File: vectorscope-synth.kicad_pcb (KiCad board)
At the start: 2 copper layers, 116 x 73 mm, 25 parts, among them J1 STYLUS, J2 IO CONNECTOR, J2OUT IO CONNECTOR, J3 SCOPE, J3OUT SCOPE, J4 SIGGEN, J4OUT SIGGEN, J5 PATCH SELECT, J6 WRITE PATCH, J7 PARAM SELECT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

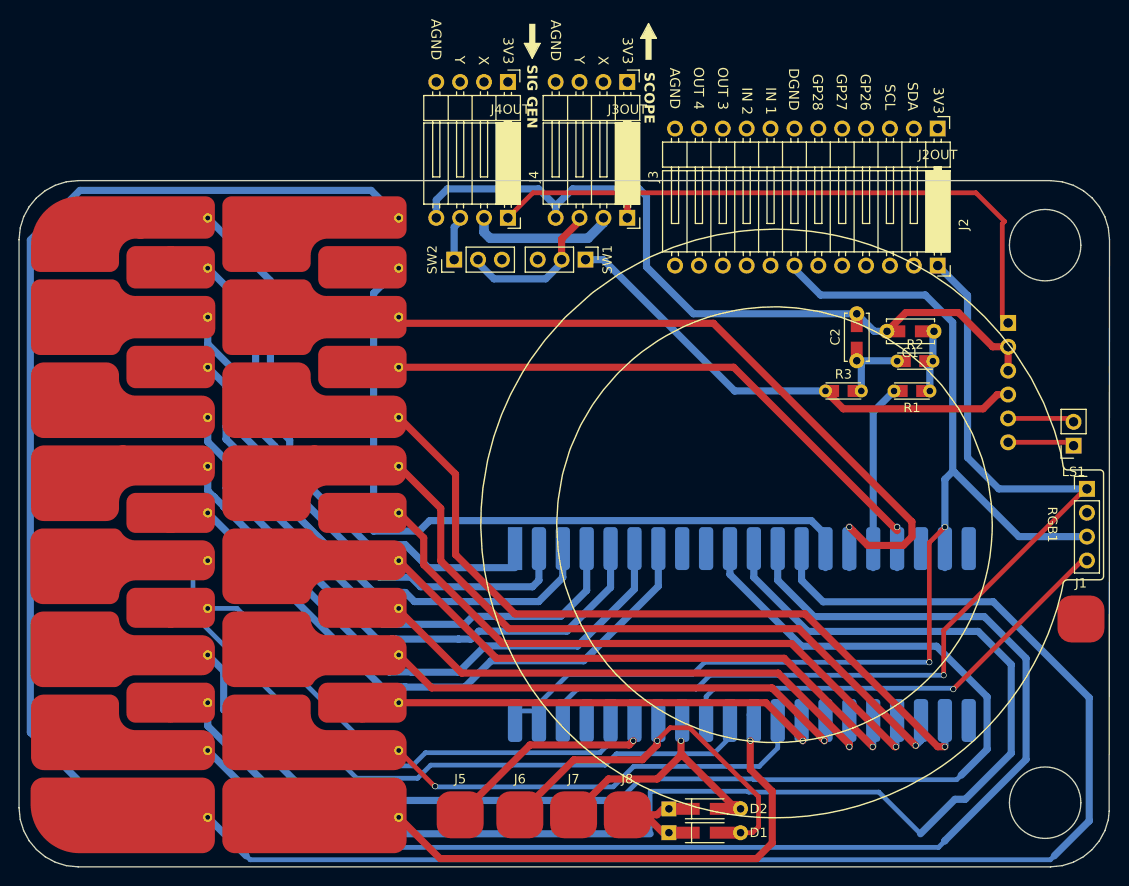
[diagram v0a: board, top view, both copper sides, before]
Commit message: Added op amp LM358 circuit to move PWM levels to vectorscope 0-3.3v. Replaced XH-M125/XPT8871 amp with GF1002/PAM8403 stereo amp with volume control. Enlarged many traces. Added logos for SoftEgg and Aisler. Learned that none of our passives or opamps had been ordered. Learned that our supplier only has 9 LED rings. Continued panicing...
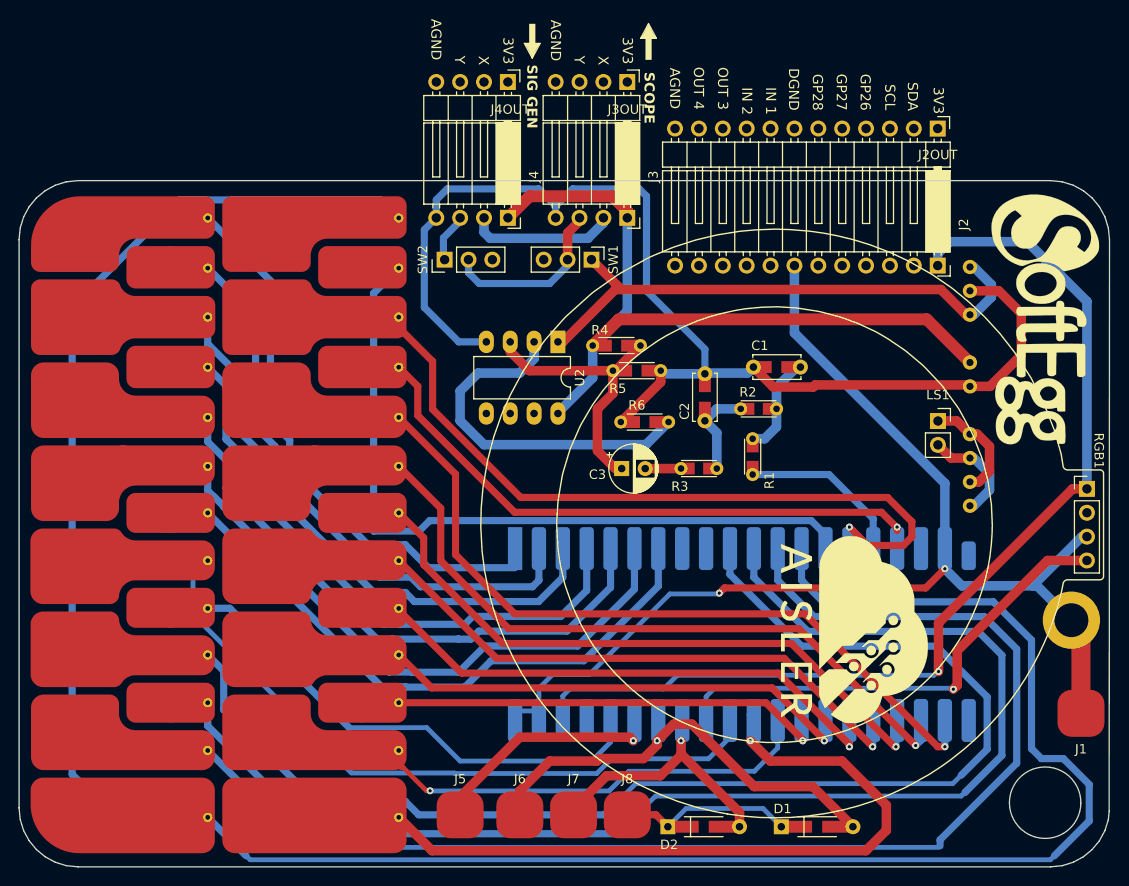
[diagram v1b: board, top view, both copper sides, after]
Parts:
- added ?: , , F.Cu at (202.4, 115.3)
- added C3: 10uF, Capacitor_THT:CP_Radial_D5.0mm_P2.50mm, F.Cu at (154.6, 99.1)
- added G***: LOGO, SoftEggKiCAD:Aisler Cloud BW 20mm, F.Cu at (178.4, 116.3)
- added G***: LOGO, SoftEggKiCAD:SOFTEGG_LOGO2, F.Cu at (199.7, 83.3)
- added G***: LOGO, SoftEggKiCAD:SOFTEGG_LOGO, B.Cu at (123.5, 106.1)
- added G***: LOGO, SoftEggKiCAD:Aisler Cloud BW 20mm, B.Cu at (98.7, 106.1)
- added R4: 200k, SoftEggKiCAD:R_Axial_DIN0204_L3.6mm_D1.6mm_P5mm_Horizontal+SMD804, F.Cu at (150.3, 86.1)
- added R5: 3.3k, SoftEggKiCAD:R_Axial_DIN0204_L3.6mm_D1.6mm_P5mm_Horizontal+SMD804, F.Cu at (152.4, 88.7)
- added R6: 1k, SoftEggKiCAD:R_Axial_DIN0204_L3.6mm_D1.6mm_P5mm_Horizontal+SMD804, F.Cu at (153.2, 94.2)
- added U2: LM358, Package_DIP:DIP-8_W7.62mm_LongPads, F.Cu at (147.8, 85.7)
- AMP1: footprint SoftEggKiCAD:XH-M125 Amplifier Board -> SoftEggKiCAD:GF1002-PAM8403_Amplifier_Module
- moved R1 21.0 mm to (168.5, 94.1), turned to -90 degrees
- moved AMP1 19.9 mm to (191.7, 103.1), turned to 0 degrees
- moved R3 17.4 mm to (159.0, 99.1)
- moved R2 17.4 mm to (165.4, 92.8)
- moved C2 17.4 mm to (163.5, 94.1)
- moved C1 14.7 mm to (173.6, 88.3)
- moved LS1 14.7 mm to (188.2, 94.1), turned to 0 degrees
- moved D1 12.0 mm to (171.6, 137.2)
- moved J1 10.0 mm to (203.5, 125.2)
- moved D2 1.91 mm to (159.5, 137.2)
- moved SW2 1.02 mm to (135.8, 76.9)
- moved SW1 0.64 mm to (151.4, 76.9)
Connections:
- AMP1 pad 1: /3V3F -> Net-(AMP1-LOUT+)
- AMP1 pad 2: GNDA -> Net-(AMP1-LOUT-)
- AMP1 pad 3: GNDA -> Net-(AMP1-LOUT+)
- AMP1 pad 4: /PWM_OUT -> Net-(AMP1-LOUT-)
- AMP1 pad 5: Net-(AMP1-OUT-) -> GNDA
- AMP1 pad 6: Net-(AMP1-OUT+) -> /3V3F
- J1 pad 1: GND -> /DGND
- LS1 pad 1: Net-(AMP1-OUT+) -> Net-(AMP1-LOUT-)
- LS1 pad 2: Net-(AMP1-OUT-) -> Net-(AMP1-LOUT+)
- R1 pad 2: /AUDIO_OUT -> /PWM_OUT
- R3 pad 1: /PWM_OUT -> /AUDIO_LOW
- SW1 pad 1: /PWM_OUT -> /AUDIO_HIGH
- U1 pad 16: /AUDIO_OUT -> /PWM_OUT
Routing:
- net /AUDIO_HIGH: track 0.00 -> 59.2 mm
- net GNDA: track 81.6 -> 126.8 mm
- net Net-(U2A--): track 0.00 -> 38.5 mm
- net /PWM_OUT: track 52.2 -> 19.5 mm
- net Net-(U2A-+): track 0.00 -> 29.4 mm
- net /C2: track 57.4 -> 77.6 mm
- net /AUDIO_OUT: track 19.7 -> 0.00 mm
- net /3V3F: track 69.0 -> 82.1 mm
- net Net-(AMP1-LOUT-): track 0.00 -> 11.8 mm
- net Net-(D1-K): track 9.54 -> 21.3 mm
- net Net-(AMP1-LOUT+): track 0.00 -> 11.3 mm
- net /C1: track 265.2 -> 255.2 mm
- net /WRITE: track 38.0 -> 45.7 mm
- net /A#0: track 144.3 -> 136.7 mm
- net Net-(AMP1-OUT-): track 7.11 -> 0.00 mm
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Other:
- outline, holes or cut-outs redrawn
- rule pad_to_mask_clearance: 0.1016 -> 0
- board text added: "Boards produced by"
- board text added: "Design by at"
- board text added: "Tinabel"

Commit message: PCB and Schematic updates by Thea @ Aisler
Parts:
- removed SW1, SW2: SW_SPST, Connector_PinHeader_2.54mm:PinHeader_1x03_P2.54mm_Vertical
- added J9: Conn_01x02_Pin, Connector_PinHeader_2.54mm:PinHeader_1x02_P2.54mm_Vertical, F.Cu at (202.2, 71.2)
- added NT1: NetTie_3, NetTie:NetTie-3_SMD_Pad0.5mm, B.Cu at (197.8, 77.2)
- added R7: 200k, Diode+THT+SMD:R_Axial_DIN0204_L3.6mm_D1.6mm_P7.62mm_Horizontal+SMD804, F.Cu at (136.7, 85.4)
- added R8: 200k, Diode+THT+SMD:R_Axial_DIN0204_L3.6mm_D1.6mm_P7.62mm_Horizontal+SMD804, F.Cu at (186.2, 90.0)
- added SW3: SW_SPDT, Connector_PinHeader_2.54mm:PinHeader_1x03_P2.54mm_Vertical, F.Cu at (193.2, 71.2)
- added SW4: SW_SPDT, Connector_PinHeader_2.54mm:PinHeader_1x03_P2.54mm_Vertical, F.Cu at (137.3, 77.2)
- moved R6 18.9 mm to (138.8, 82.0)
- moved R4 9.79 mm to (160.0, 85.8), turned to 180 degrees
- moved G*** 5.70 mm to (199.7, 89.0)
- moved C3 5.67 mm to (156.3, 93.7)
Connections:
- AMP1 pad 1: Net-(AMP1-LOUT+) -> Net-(AMP1-ROUT)
- AMP1 pad 2: Net-(AMP1-LOUT-) -> Net-(AMP1-ROUT-)
- AMP1 pad 3: Net-(AMP1-LOUT+) -> unconnected-(AMP1-LOUT+-Pad3)
- AMP1 pad 4: Net-(AMP1-LOUT-) -> unconnected-(AMP1-LOUT--Pad4)
- AMP1 pad 6: /3V3F -> +3.3V
- AMP1 pad 7: /AUDIO_HIGH -> Net-(AMP1-L)
- J2 pad 1: +3.3V -> /+3.3V-IN
- J2 pad 7: /DGND -> /GND-IN
- J3 pad 1: /3V3F -> unconnected-(J3-Pin_1-Pad1)
- J4 pad 1: /3V3F -> unconnected-(J4-Pin_1-Pad1)
- LS1 pad 1: Net-(AMP1-LOUT-) -> Net-(AMP1-ROUT-)
- LS1 pad 2: Net-(AMP1-LOUT+) -> Net-(AMP1-ROUT)
- R4 pad 1: /3V3F -> +3.3V
- U1 pad 18: +5V -> unconnected-(U1-5V-Pad18)
- U2 pad 5: (no net) -> Net-(U2B-+)
- U2 pad 6: (no net) -> Net-(U2B--)
- U2 pad 7: (no net) -> Net-(U2B--)
- U2 pad 8: /3V3F -> +3.3V
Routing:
- net GNDA: track 126.8 -> 2.19 mm, vias 0 -> 11
- net /DGND: track 126.1 -> 16.0 mm, vias 2 -> 17
- net /3V3F: track 82.1 -> 0.00 mm
- net +3.3V: track 109.4 -> 167.1 mm, vias 1 -> 3
- net /GND-IN: track 0.00 -> 35.1 mm
- net Net-(U2A--): track 38.5 -> 3.77 mm
- net Net-(AMP1-ROUT-): track 0.00 -> 15.2 mm
- net Net-(AMP1-LOUT-): track 11.8 -> 0.00 mm
- net Net-(AMP1-LOUT+): track 11.3 -> 0.00 mm
- net /+3.3V-IN: track 0.00 -> 9.97 mm
- net Net-(AMP1-ROUT): track 0.00 -> 8.94 mm
- net Net-(U2A-+): track 29.4 -> 23.4 mm
- net Net-(AMP1-L): track 0.00 -> 5.58 mm
- net /SCOPE_Y: track 18.8 -> 14.5 mm
- net Net-(J9-Pin_1): track 0.00 -> 3.97 mm
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- added copper zone on B.Cu, net /DGND
- added copper zone on F.Cu, net /DGND
- added copper zone on B.Cu, net GNDA
- added copper zone on F.Cu, net GNDA
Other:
- board text added: "+"
- board text added: "-"
- board text added: "Audio"
- board text added: "Badge"
- board text added: "Batt"
- board text added: "Gen."
- board text added: "Speaker"

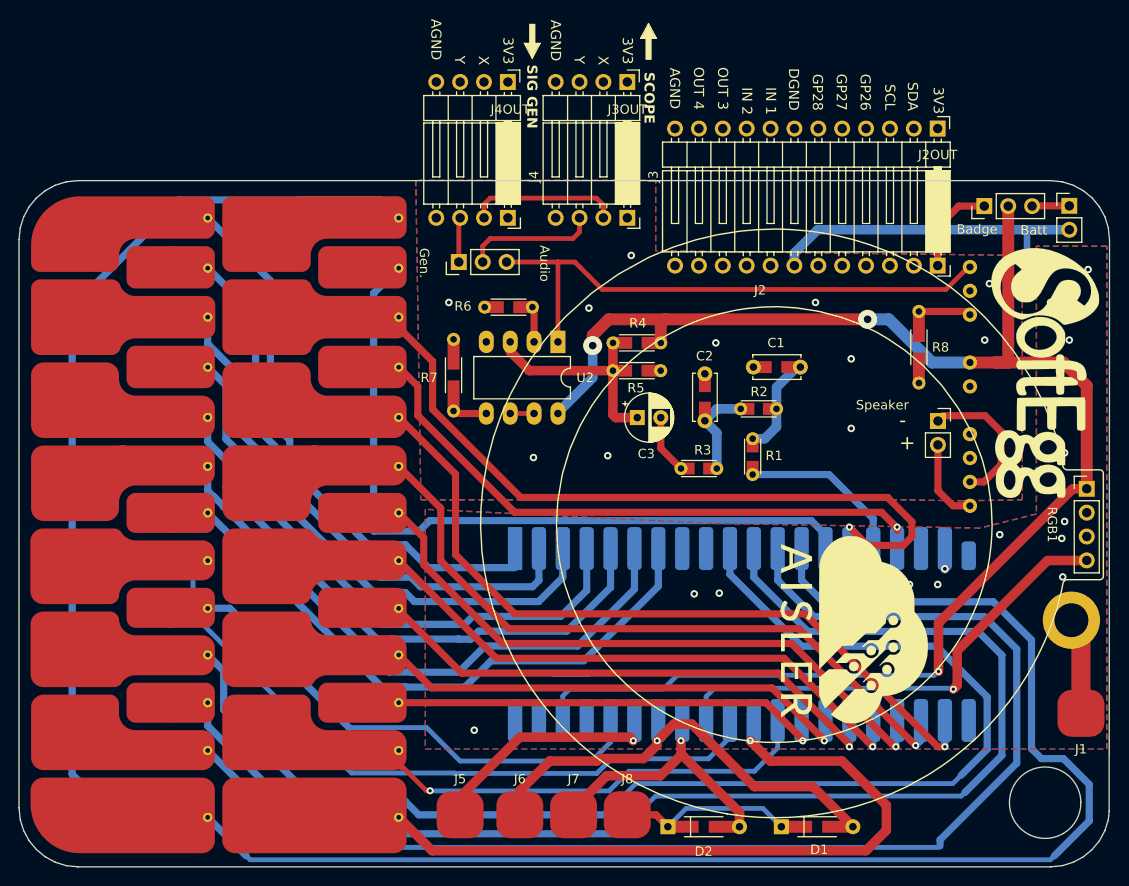
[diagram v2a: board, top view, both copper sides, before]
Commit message: Note: This is NOT the version used in the Hackaday Europe 2024 Workshop, that is the previous version. This is a version that fixes the LED ring wiring problem with that one, and has a footprint that more correctly shows the size of that LED ring. There may still be other issues... I'll find out when I go to build one from that PCB tomorrow.
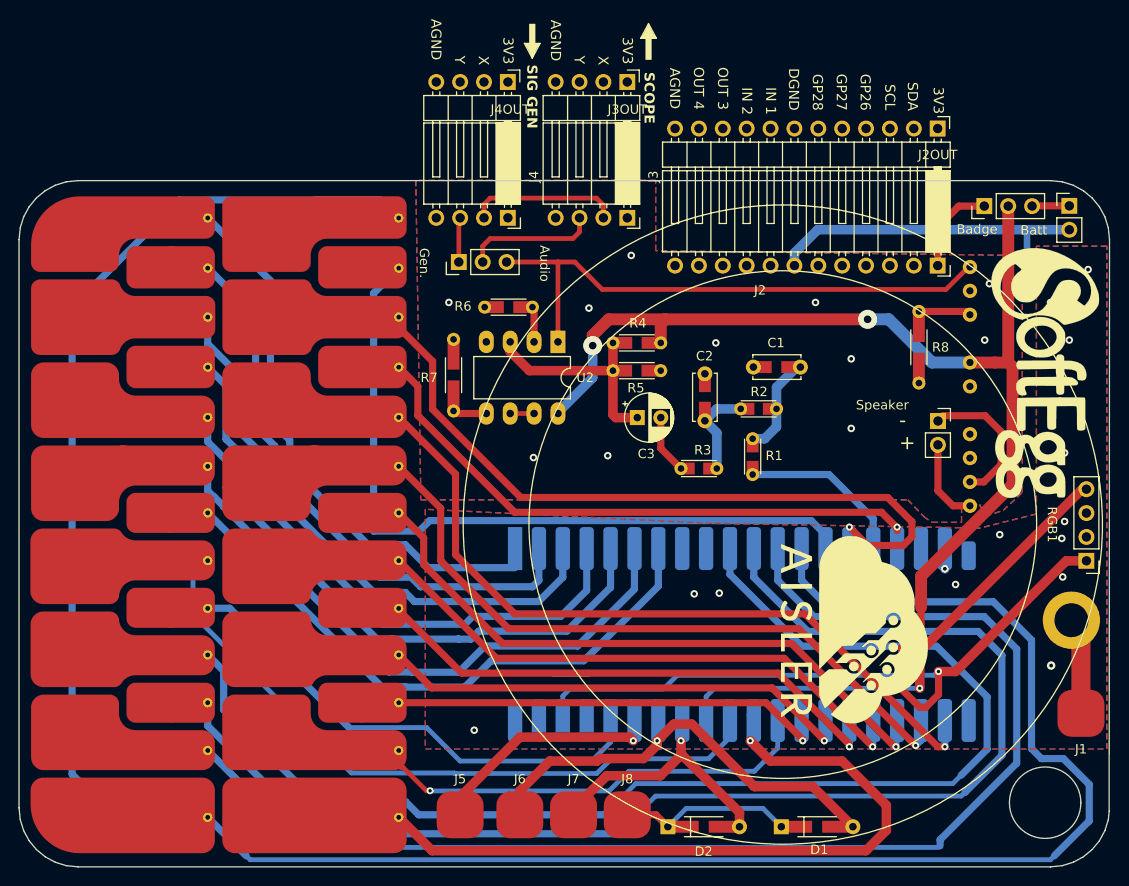
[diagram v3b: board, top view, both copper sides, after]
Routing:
- net +3.3V: track 167.1 -> 186.5 mm
- net /LED_DIN: track 49.8 -> 52.9 mm
- net /DGND: vias 17 -> 18

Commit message: Changed Resstor to give good values for the vector scope. Updated headers to give proper credits.
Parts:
- R5: value 3.3k -> 33k
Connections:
- RGB1 pad 1: +3.3V -> /LED_DIN
- RGB1 pad 2: unconnected-(RGB1-DOUT-Pad2) -> +3.3V
- RGB1 pad 4: /LED_DIN -> unconnected-(RGB1-DOUT-Pad4)
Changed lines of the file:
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@@
 	(title_block
 		(title "VectorScope Badge Synthesizer")
-		(date "2024-04-08")
-		(rev "0.3")
+		(date "2024-04-11")
+		(rev "0.4")
 		(company "SoftEgg")
-		(comment 1 "Version 0.2 - T. B. Trzepacz 7/4/24")
-		(comment 2 "Version 0.3 - Thea @ Aisler 8/4/24")
+		(comment 1 "Version 0.2 - T. B. Trzepacz 2024-4-7")
+		(comment 2 "Version 0.3 - Thea @ Aisler 2024-4-8")
+		(comment 3 "Version 0.4 - T.B. Trzepacz 2024-4-11")
 		(comment 4 "AISLER Project ID: WYZHWGMS")
 	)
@@
 	(net 63 "Net-(D1-K)")
 	(net 64 "/PWM_OUT")
-	(net 65 "unconnected-(RGB1-DOUT-Pad2)")
+	(net 65 "unconnected-(RGB1-DOUT-Pad4)")
 	(net 66 "Net-(U2A-+)")
 	(net 67 "/AUDIO_LOW")
@@
 			)
 		)
-		(property "Value" "3.3k"
+		(property "Value" "33k"
 			(at 5.588 1.905 0)
 			(layer "F.Fab")
@@
 			)
 		)
+		(sheetname "Root")
+		(sheetfile "vectorscope-synth.kicad_sch")
 		(attr through_hole)
 		(fp_line
@@
 			(layers "*.Cu" "*.Mask")
 			(remove_unused_layers no)
-			(net 20 "+3.3V")
-			(pinfunction "VDD")
-			(pintype "power_in")
+			(net 56 "/LED_DIN")
+			(pinfunction "DIN")
+			(pintype "input")
 		)
 		(pad "2" thru_hole oval
@@
 			(layers "*.Cu" "*.Mask")
 			(remove_unused_layers no)
-			(net 65 "unconnected-(RGB1-DOUT-Pad2)")
-			(pinfunction "DOUT")
-			(pintype "output+no_connect")
+			(net 20 "+3.3V")
+			(pinfunction "VDD")
+			(pintype "power_in")
 		)
 		(pad "3" thru_hole oval
@@
 			(layers "*.Cu" "*.Mask")
 			(remove_unused_layers no)
-			(net 56 "/LED_DIN")
-			(pinfunction "DIN")
-			(pintype "input")
+			(net 65 "unconnected-(RGB1-DOUT-Pad4)")
+			(pinfunction "DOUT")
+			(pintype "output+no_connect")
 		)
 	)

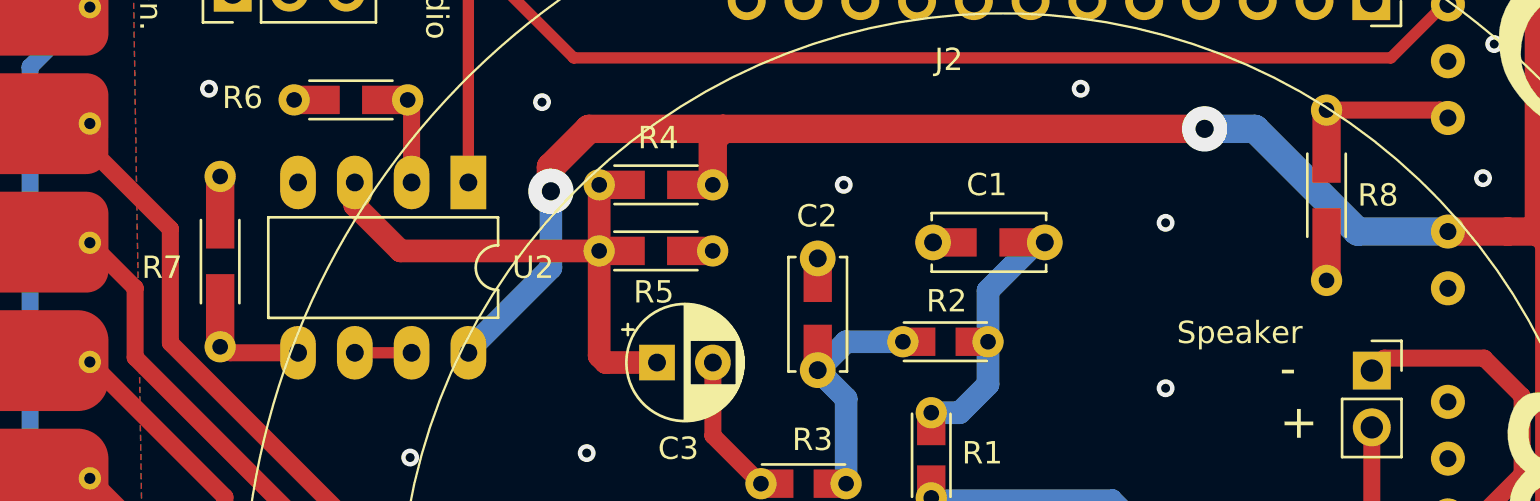
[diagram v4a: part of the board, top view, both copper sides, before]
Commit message: Enlarged holes for amplifier PCB mounting. Updated PCB pics and Schematic PDF to match revisions.
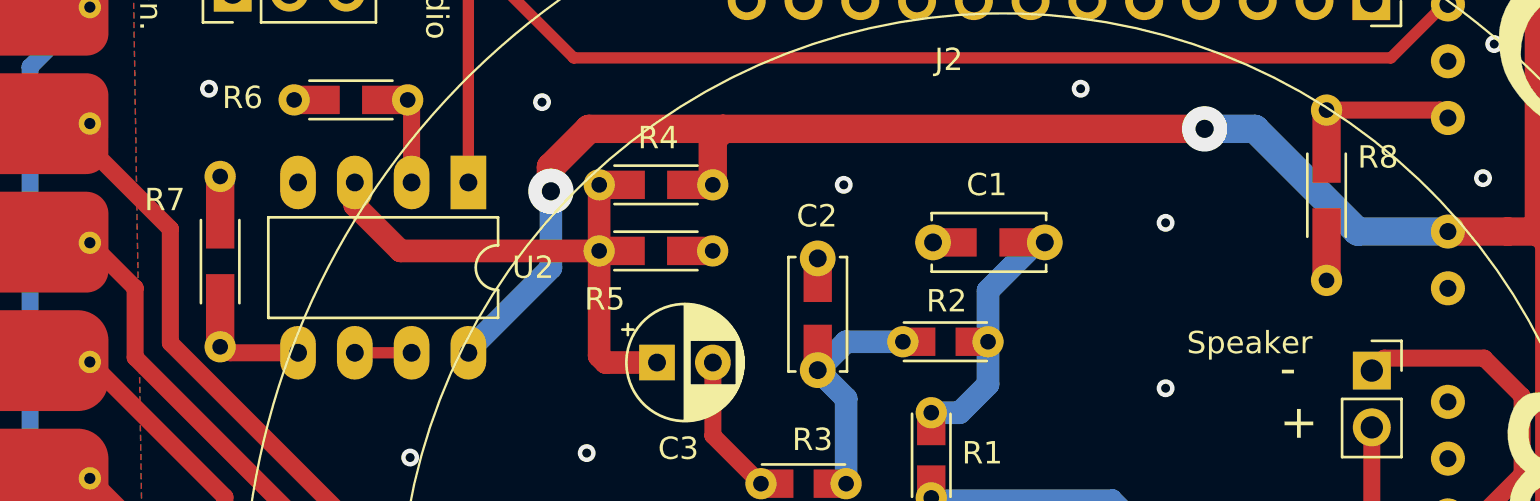
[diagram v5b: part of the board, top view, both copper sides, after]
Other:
- board text added: "X DGND +3.3V LED_DIN"
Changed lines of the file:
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@@
 			(at 0 4.87 0)
 			(layer "F.Fab")
+			(hide yes)
 			(effects
 				(font
@@
 		)
 		(fp_text user "${REFERENCE}"
-			(at 0 1.270001 90)
+			(at 3.145 1.91 180)
 			(layer "F.Fab")
 			(effects
@@
 		)
 		(property "Value" "LM358"
-			(at 3.81 9.95 90)
+			(at 3.825 3.8 180)
 			(layer "F.Fab")
 			(effects
@@
 		)
 		(fp_text user "${REFERENCE}"
-			(at 3.81 3.81 90)
+			(at 2.682 7.229 180)
 			(layer "F.Fab")
 			(effects
@@
 		)
 		(property "Value" "33kΩ"
-			(at 5.207 1.905 0)
+			(at 3.81 1.905 0)
 			(layer "F.Fab")
 			(effects
@@
 		(tags "Resistor Axial_DIN0204 series Axial Horizontal pin pitch 7.62mm 0.16666666666666666W = 1/6W length 3.6mm diameter 1.6mm")
 		(property "Reference" "R7"
-			(at 4.074999 2.6 180)
+			(at 1.044999 2.475 180)
 			(layer "F.SilkS")
 			(effects
@@
 		(tags "Resistor Axial_DIN0204 series Axial Horizontal pin pitch 7.62mm 0.16666666666666666W = 1/6W length 3.6mm diameter 1.6mm")
 		(property "Reference" "R5"
-			(at 3.714 1.844 0)
+			(at 1.524 2.159 0)
 			(layer "F.SilkS")
 			(effects
@@
 		)
 		(property "Value" "33k"
-			(at 5.588 1.905 0)
+			(at 3.71 0 0)
 			(layer "F.Fab")
 			(effects
@@
 		)
 		(property "Value" "220nF"
-			(at 0.635 2.286 0)
+			(at -1.27 2.54 0)
 			(layer "F.Fab")
 			(effects
@@
 		)
 		(fp_text user "${REFERENCE}"
-			(at 4.318 2.286 0)
+			(at 2.54 2.54 0)
 			(layer "F.Fab")
 			(effects
@@
 		)
 		(property "Value" "SW_SPDT"
-			(at 0 7.41 -90)
+			(at 3.83 3.295 0)
 			(layer "F.Fab")
 			(effects
@@
 		)
 		(fp_text user "${REFERENCE}"
-			(at 0 2.54 0)
+			(at 1.925 -0.515 0)
 			(layer "F.Fab")
 			(effects
@@
 		)
 		(property "Value" "3.3kΩ"
-			(at 6.223 -1.778 0)
+			(at 8.89 0 0)
 			(layer "F.Fab")
 			(effects
@@
 		(tags "Resistor Axial_DIN0204 series Axial Horizontal pin pitch 7.62mm 0.16666666666666666W = 1/6W length 3.6mm diameter 1.6mm")
 		(property "Reference" "R8"
-			(at 3.81 2.3 0)
+			(at 5.51 2.3 0)
 			(layer "F.SilkS")
 			(effects
@@
 		)
 		(property "Value" "200k"
-			(at 3.81 1.905 -90)
+			(at 3.605 3.27 0)
 			(layer "F.Fab")
 			(effects
@@
 		)
 		(property "Value" "1N4148"
-			(at 5.207 1.905 0)
+			(at 5.207 -1.905 0)
 			(layer "F.Fab")
 			(effects
@@
 		)
 		(property "Value" "LED_Ring_16_WS2812B"
-			(at 3.673 5.207 -90)
+			(at -2.911808 -7.259 0)
 			(unlocked yes)
 			(layer "F.Fab")
@@
 		)
 		(property "Value" "200k"
-			(at 5.461 -1.651 180)
+			(at 3.71 0 180)
 			(layer "F.Fab")
 			(effects
@@
 		)
 		(property "Value" "330Ω"
-			(at 3.302 -1.905 90)
+			(at 5.08 -3.81 180)
 			(layer "F.Fab")
 			(effects
@@
 		)
 		(property "Value" "SW_SPDT"
-			(at 0 7.41 -90)
+			(at -2.285 2.045 0)
 			(layer "F.Fab")
 			(effects
@@
 	)
 	(gr_text "Speaker"
-		(at 179.52365 92.9643 0)
+		(at 179.96865 93.4193 0)
 		(layer "F.SilkS")
 		(effects
@@
 		)
 	)
+	(gr_text "X\nDGND\n+3.3V\nLED_DIN"
+		(at 206.63865 105.2303 0)
+		(layer "F.Fab")
+		(effects
+			(font
+				(size 1.65 1.5)
+				(thickness 0.3)
+				(bold yes)
+			)
+			(justify left)
+		)
+	)
